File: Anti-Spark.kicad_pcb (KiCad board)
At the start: 2 copper layers, 74 x 38.2 mm, 18 parts, among them IC1 BQ76200PWR, IC2 TPS7A4101DGNR, J1 Conn_01x04_Male, Q1 IRFS7530TRL7PP, Q2 IRFS7530TRL7PP

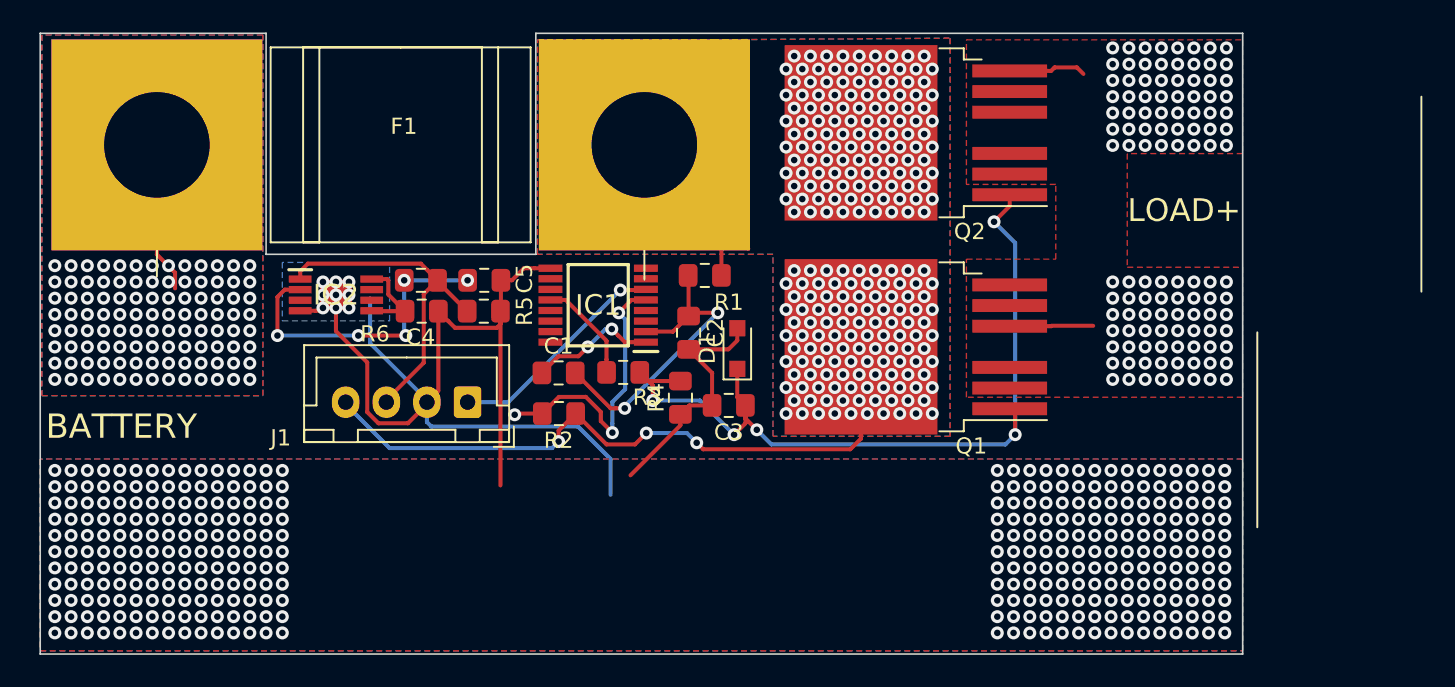
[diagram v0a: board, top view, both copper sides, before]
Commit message: add: gnd plane for logic
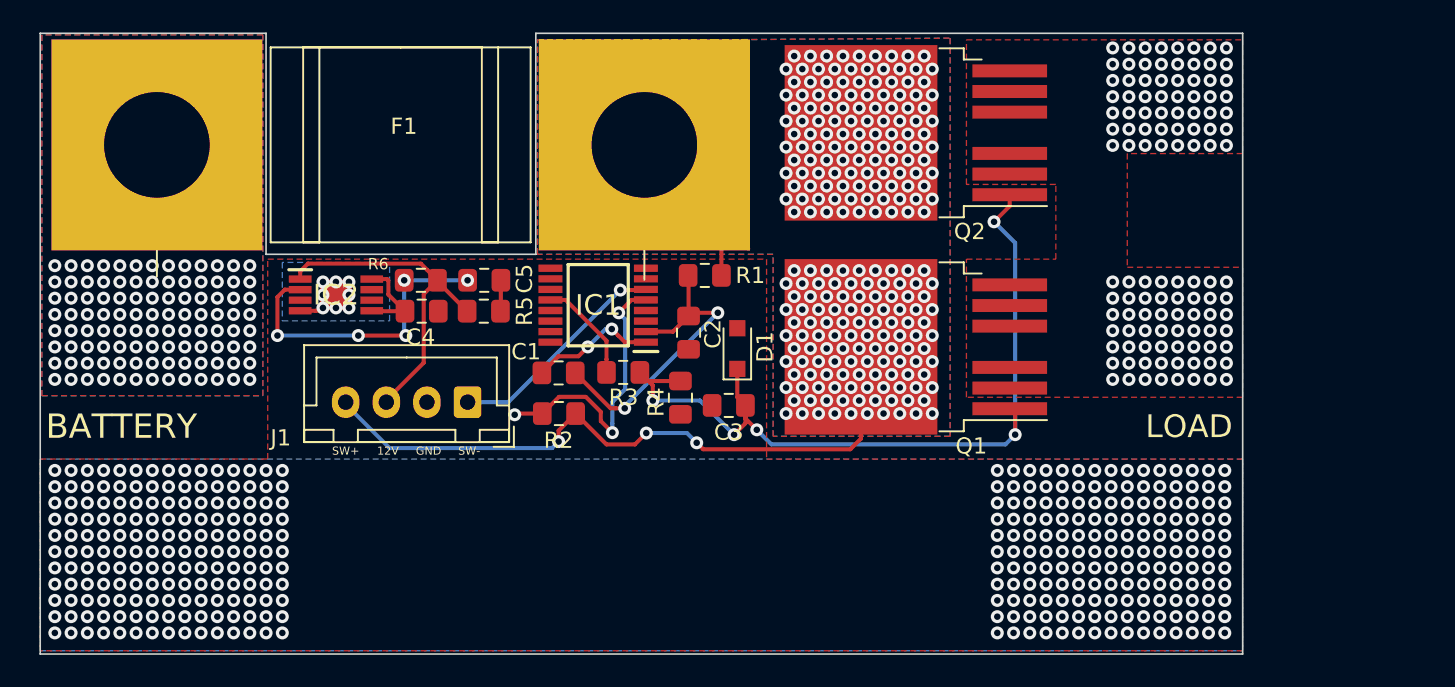
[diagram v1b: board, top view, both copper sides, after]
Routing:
- net -BATT: track 81.0 -> 4.51 mm, vias 339 -> 338
- net VESC: track 9.94 -> 0.00 mm
- net SW+: track 50.9 -> 41.6 mm
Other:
- board text added: "12V"
- board text added: "GND"
- board text added: "LOAD"
- board text added: "SW+"
- board text added: "SW-"
- board text removed: "LOAD+"

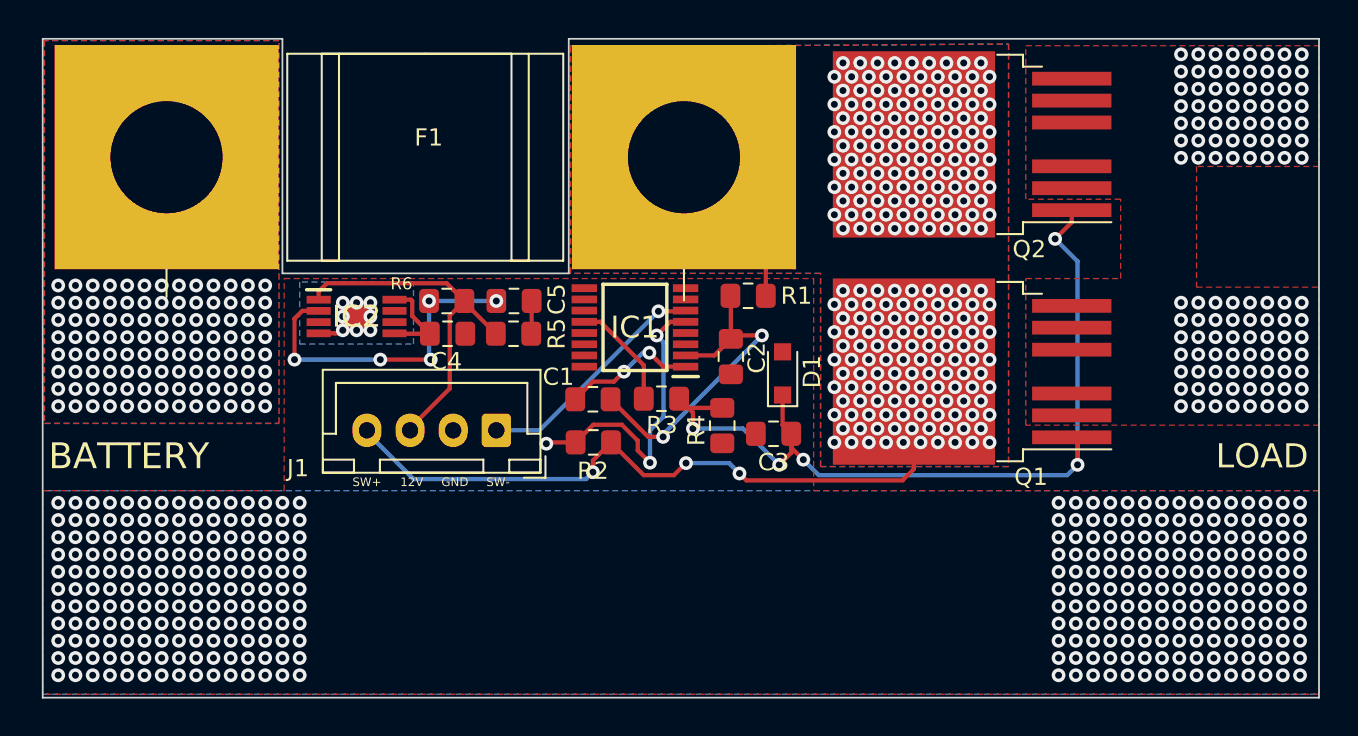
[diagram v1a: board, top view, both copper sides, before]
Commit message: ch: new version with 10 mosfets
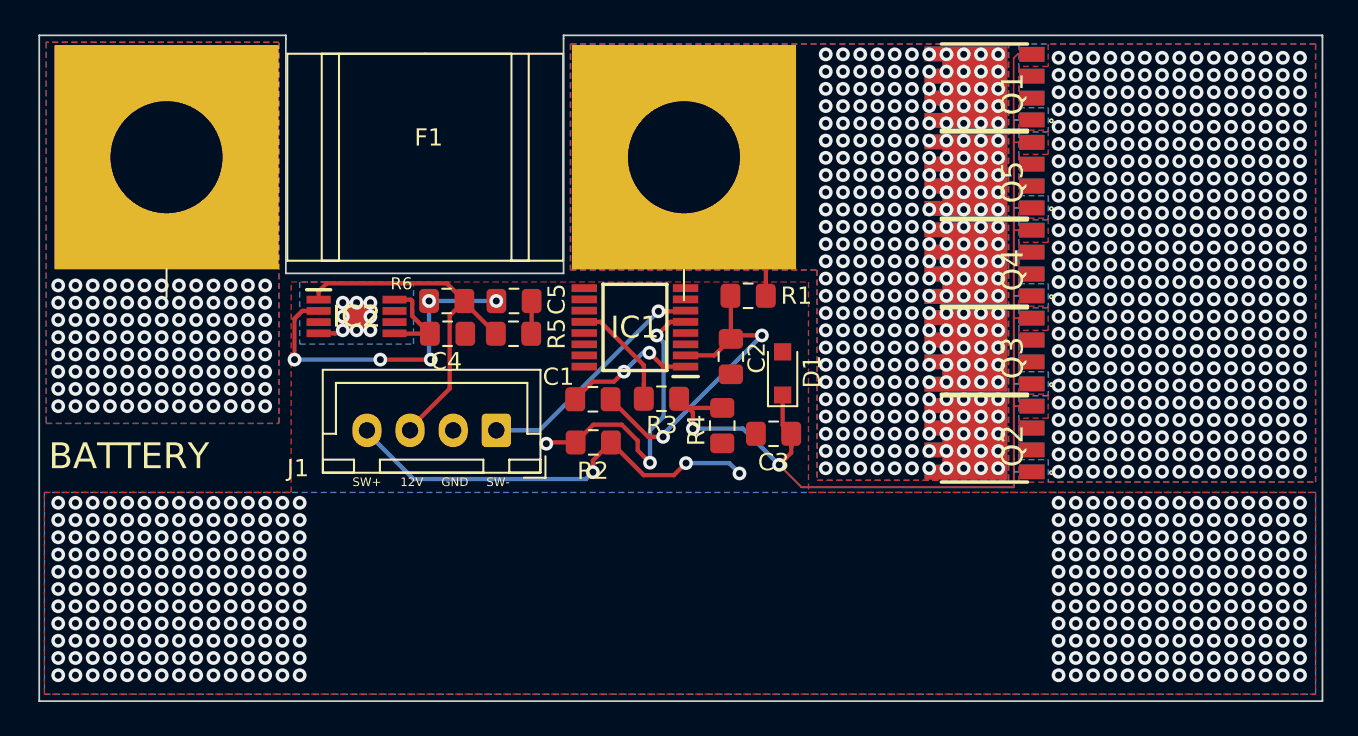
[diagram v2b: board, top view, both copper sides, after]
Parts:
- added Q10: TPW1R306PL,L1Q, SamacSys_Parts:SOP_ADVANCE, B.Cu at (127.7, 54.2)
- added Q3: TPW1R306PL,L1Q, SamacSys_Parts:SOP_ADVANCE, F.Cu at (127.7, 54.2)
- added Q4: TPW1R306PL,L1Q, SamacSys_Parts:SOP_ADVANCE, F.Cu at (127.7, 49.1)
- added Q5: TPW1R306PL,L1Q, SamacSys_Parts:SOP_ADVANCE, F.Cu at (127.7, 44.0)
- added Q6: TPW1R306PL,L1Q, SamacSys_Parts:SOP_ADVANCE, B.Cu at (127.7, 38.9)
- added Q7: TPW1R306PL,L1Q, SamacSys_Parts:SOP_ADVANCE, B.Cu at (127.7, 49.1)
- added Q8: TPW1R306PL,L1Q, SamacSys_Parts:SOP_ADVANCE, B.Cu at (127.7, 44.0)
- added Q9: TPW1R306PL,L1Q, SamacSys_Parts:SOP_ADVANCE, B.Cu at (127.7, 59.3)
- Q1, Q2: value IRFS7530TRL7PP -> TPW1R306PL,L1Q; footprint SamacSys_Parts:IRFS7530 -> SamacSys_Parts:SOP_ADVANCE
- moved Q2 17.1 mm to (127.7, 59.3), turned to 90 degrees
- moved Q1 16.5 mm to (127.7, 38.9), turned to 90 degrees
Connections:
- F1 pad 1: Net-(F1-Pad1) -> FUSE+
- F1 pad 2: SW+ -> BATT+
- Q1 pad 1: Net-(C3-Pad1) -> VESC
- Q1 pad 5: VESC -> FUSE+
- Q1 pad 6: VESC -> FUSE+
- Q1 pad 7: VESC -> FUSE+
- Q1 pad 8: SW+ -> FUSE+
- Q2 pad 1: Net-(C3-Pad1) -> VESC
- Q2 pad 5: VESC -> FUSE+
- Q2 pad 6: VESC -> FUSE+
- Q2 pad 7: VESC -> FUSE+
- Q2 pad 8: SW+ -> FUSE+
- R1 pad 1: Net-(F1-Pad1) -> FUSE+
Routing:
- net Net-(C3-Pad1): track 51.0 -> 101.1 mm, vias 5 -> 2
- net FUSE+: track 0.00 -> 32.4 mm, vias 0 -> 275
- net Net-(F1-Pad1): track 19.0 -> 0.00 mm
- net SW+: track 41.6 -> 25.4 mm, vias 344 -> 3
- net VESC: vias 112 -> 375
- net BATT+: vias 0 -> 104
- added copper zone on B.Cu, net BATT+
- added copper zone on F.Cu, net BATT+
- added copper zone on B.Cu, net FUSE+
- added copper zone on F.Cu, net FUSE+
- added copper zone on B.Cu, net VESC
- removed copper zone on B.Cu, net SW+
- removed copper zone on F.Cu, net SW+
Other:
- board size 74 x 38.2 mm -> 74.4 x 38.6 mm
- net class Default: clearance 0.2 -> 0.1
- net class min added: clearance 0.1, trace_width 0.1, via_dia 0.8, via_drill 0.4
- rule trace_clearance: 0.2 -> 0.1
- rule trace_min: 0.2 -> 0.1
- board text removed: "LOAD"

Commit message: updated PCB to V0.1
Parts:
- added REF**: SolderWirePad_1x01_SMD_5x10mm, SamacSys_Parts:SolderWirePad_1x01_SMD_5x10mm, F.Cu at (110.5, 60.7)
- added REF**: SolderWirePad_1x01_Drill2mm, Connector_Wire:SolderWirePad_1x01_Drill2mm, B.Cu at (143.3, 32.0)
- added REF**: SolderWirePad_1x01_Drill2mm, Connector_Wire:SolderWirePad_1x01_Drill2mm, F.Cu at (76.8, 32.0)
- added REF**: SolderWirePad_1x01_Drill2mm, Connector_Wire:SolderWirePad_1x01_Drill2mm, B.Cu at (76.8, 79.0)
- added REF**: SolderWirePad_1x01_Drill2mm, Connector_Wire:SolderWirePad_1x01_Drill2mm, F.Cu at (143.3, 79.0)
- moved Q1 4.00 mm to (131.7, 38.9)
- moved Q10 4.00 mm to (131.7, 54.2)
- moved Q2 4.00 mm to (131.7, 59.3)
- moved Q3 4.00 mm to (131.7, 54.2)
- moved Q4 4.00 mm to (131.7, 49.1)
- moved Q5 4.00 mm to (131.7, 44.0)
- moved Q6 4.00 mm to (131.7, 38.9)
- moved Q7 4.00 mm to (131.7, 49.1)
- moved Q8 4.00 mm to (131.7, 44.0)
- moved Q9 4.00 mm to (131.7, 59.3)
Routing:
- net SW+: track 25.4 -> 16.7 mm, vias 3 -> 1
- net Net-(IC1-Pad12): track 6.44 -> 12.6 mm
- net Net-(C3-Pad1): track 101.1 -> 103.4 mm, vias 2 -> 1
- net -BATT: track 4.51 -> 2.64 mm
- net FUSE+: vias 275 -> 375
- net VESC: vias 375 -> 275
- net (no net): vias 0 -> 51
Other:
- board size 74.4 x 38.6 mm -> 74.5 x 55 mm
- board text added: "AntiSpark V0.1 09.09.19"
- board text removed: "BATTERY"
